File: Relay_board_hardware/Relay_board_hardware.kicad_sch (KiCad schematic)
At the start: 6 parts, among them U1 FTR-F1A, U2 FTR-F1A

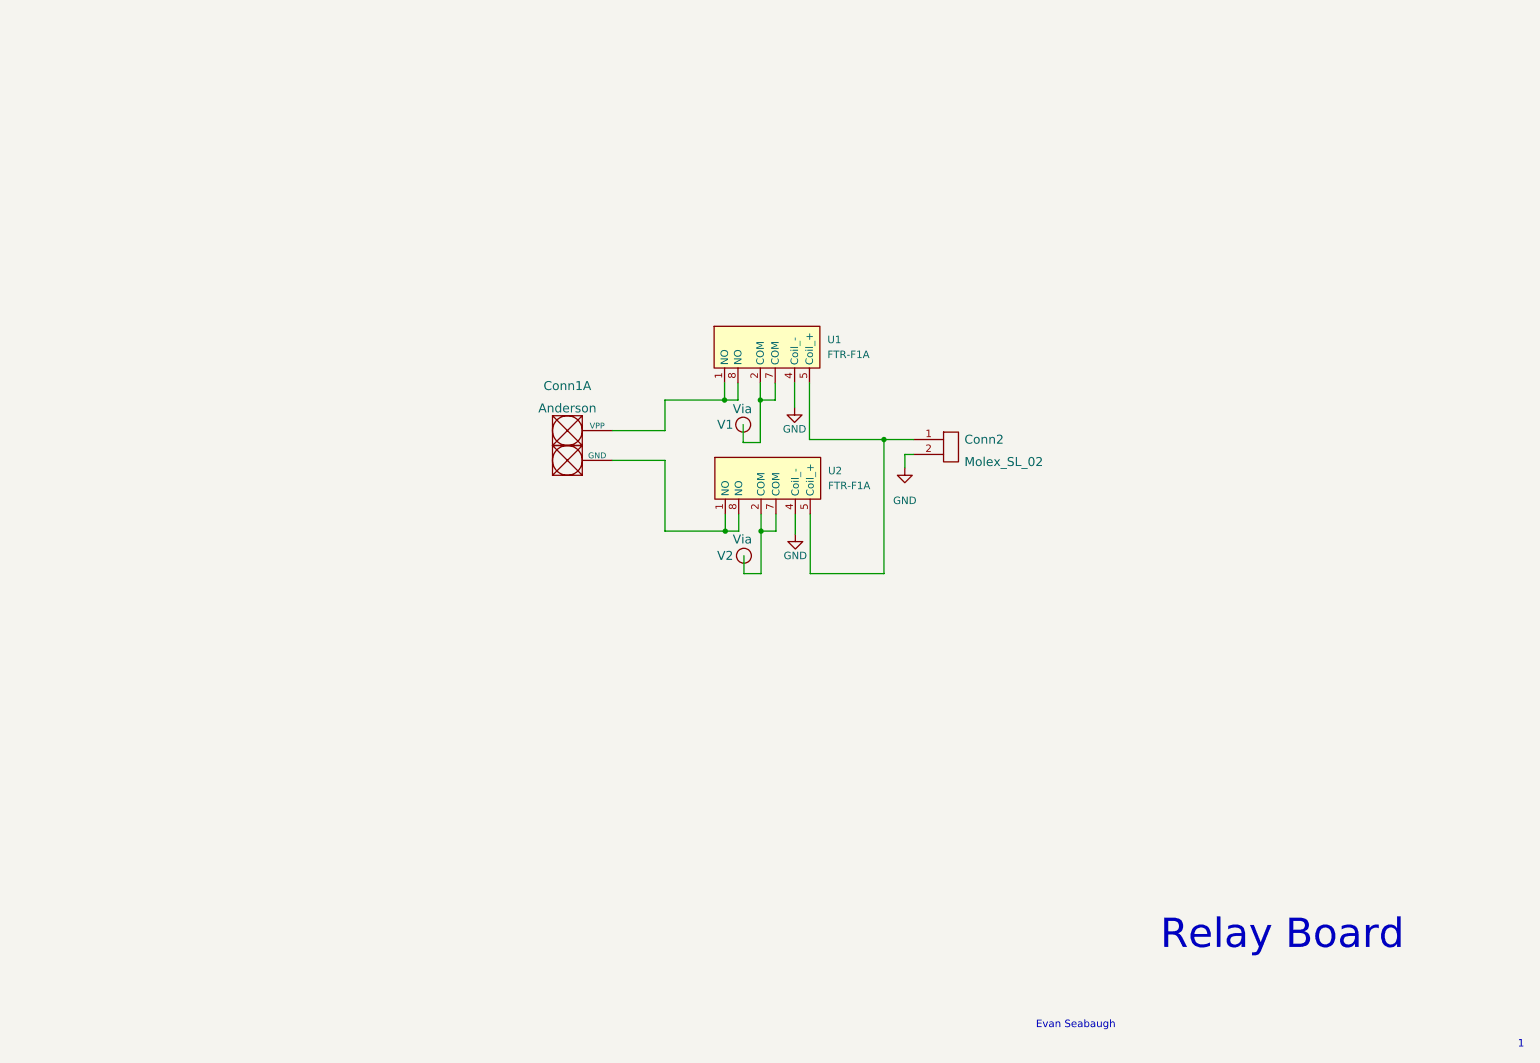
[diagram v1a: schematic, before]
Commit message: board R1
potential changes: anderson placement, IO location, warning correction
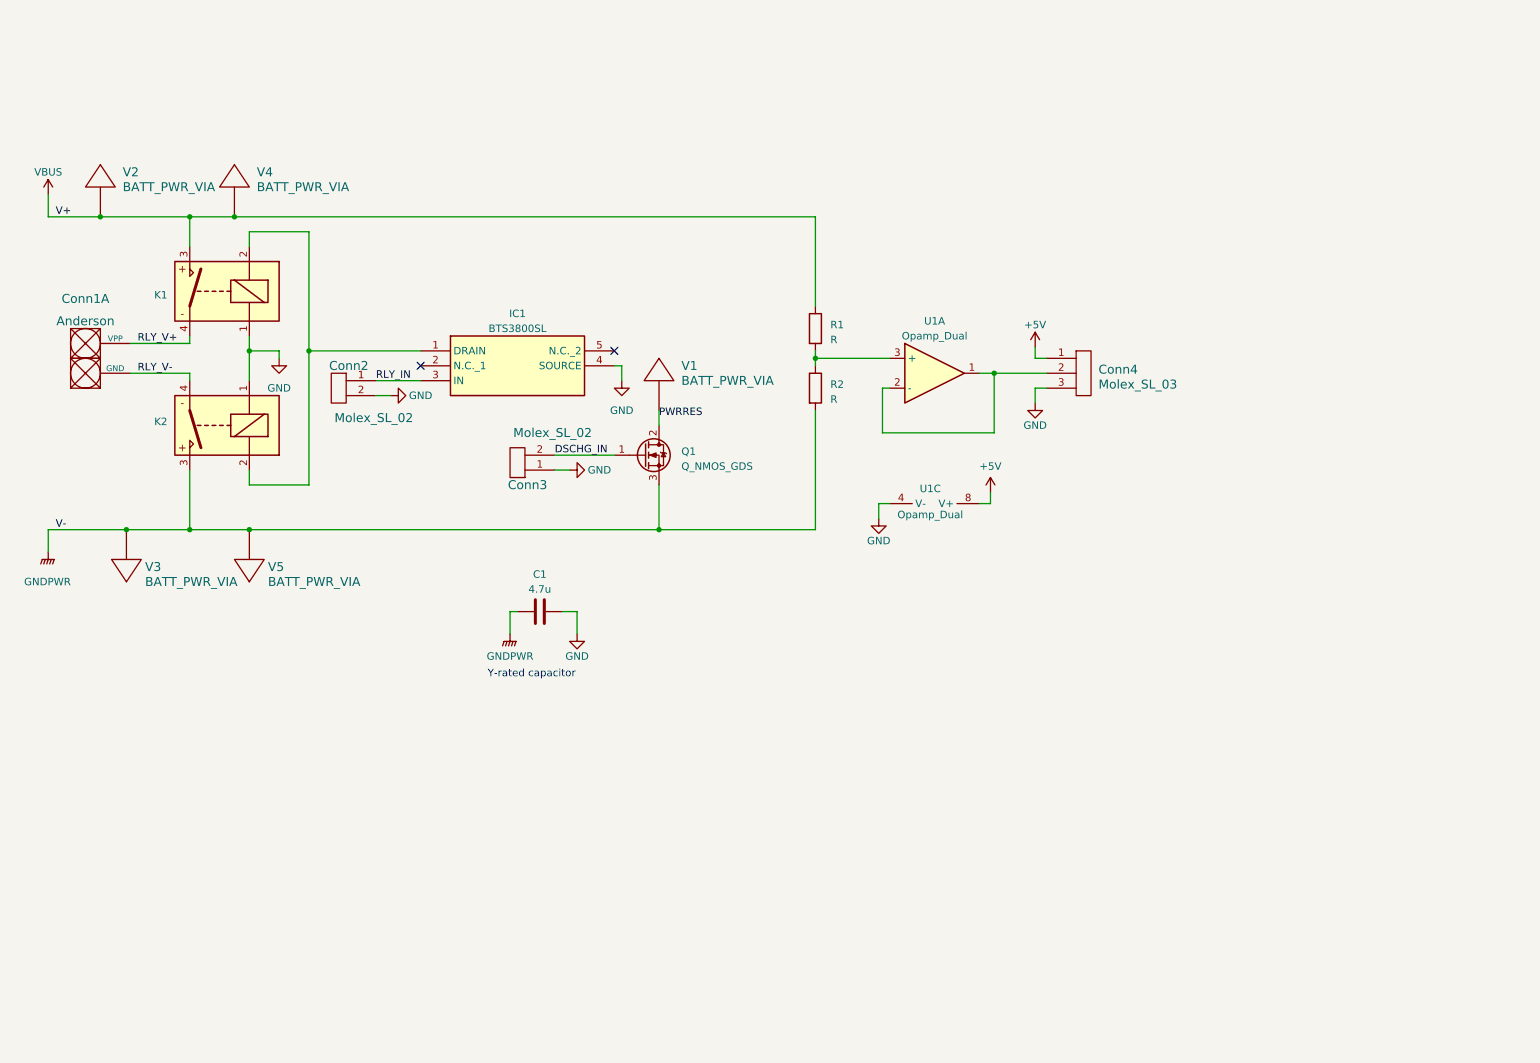
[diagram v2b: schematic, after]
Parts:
- removed Conn2: Molex_SL_02, Customs:MOLEX_SL_02_Horizontal, symbol Customs:Molex_SL_02
- removed U1, U2: FTR-F1A, Customs:FTR-F1A, symbol Customs:FTR-F1A
- removed V1, V2: Via, Customs:via, symbol Customs:Via
- added C1: 4.7u, Capacitor_THT:C_Rect_L18.0mm_W9.0mm_P15.00mm_FKS3_FKP3, symbol Device:C
- added Conn2, Conn3: Molex_SL_02, 0-customs:MOLEX_SL_02_Horizontal, symbol 0-customs:Molex_SL_02
- added Conn4: Molex_SL_03, MRDT_Connectors:MOLEX_SL_03_Horizontal, symbol MRDT_Connectors:Molex_SL_03
- added IC1: BTS3800SL, 0-customs:BTS3800SL, symbol 0-customs:BTS3800SL
- added K1, K2: ~, 0-customs:AECN11012, symbol 0-customs:AECN11012
- added Q1: Q_NMOS_GDS, Package_TO_SOT_SMD:TO-263-2, symbol Device:Q_NMOS_GDS
- added R1, R2: R, Resistor_SMD:R_2512_6332Metric_Pad1.40x3.35mm_HandSolder, symbol Device:R
- added U1: Opamp_Dual, Package_SO:SOIC-8_3.9x4.9mm_P1.27mm, symbol Device:Opamp_Dual
- added V1, V2, V3, V4, V5: BATT_PWR_VIA, 0-customs:via, symbol MRDT_Drill_Holes:BATT_PWR_VIA
- Conn1: footprint Customs:Anderson_2_Vertical_Sidy_by_Side -> 0-customs:Square_Anderson_2_V_Side_By_Side
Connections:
- net GND: now also C1.2, Conn2.2, Conn3.1, Conn4.3, IC1.4 (SOURCE), K1.1, K2.1, U1.4 (V-)
- net RLY_V+: now reaches Conn1.1 (VPP)
- net RLY_V+: now also K1.4
- net RLY_V-: now reaches Conn1.2 (GND)
- net RLY_V-: now also K2.4
- new net: Conn4.2, U1.1, U1.2 (-)
- new net: IC1.1 (DRAIN), K1.2, K2.2
- new net: R1.2, R2.1, U1.3 (+)
- new net +5V: Conn4.1, U1.8 (V+)
- new net DSCHG_IN: Conn3.2, Q1.1 (G)
- new net GNDPWR: C1.1, K2.3, Q1.3 (S), R2.2, V3.1, V5.1
- new net PWRRES: Q1.2 (D), V1.1
- new net RLY_IN: Conn2.1, IC1.3 (IN)
- new net VBUS: K1.3, R1.1, V2.1, V4.1
- no-connect marks 0 -> 2
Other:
- note added: "Y-rated capacitor"
- note removed: "1"
- note removed: "Evan Seabaugh"
- note removed: "Relay Board"
- company: (none) -> Missouri S&T
- title: (none) -> Relay and Connections Board
- moved on the sheet: Conn1A

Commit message: side-by-side-R1
complete board design with the relays situated side-by-side
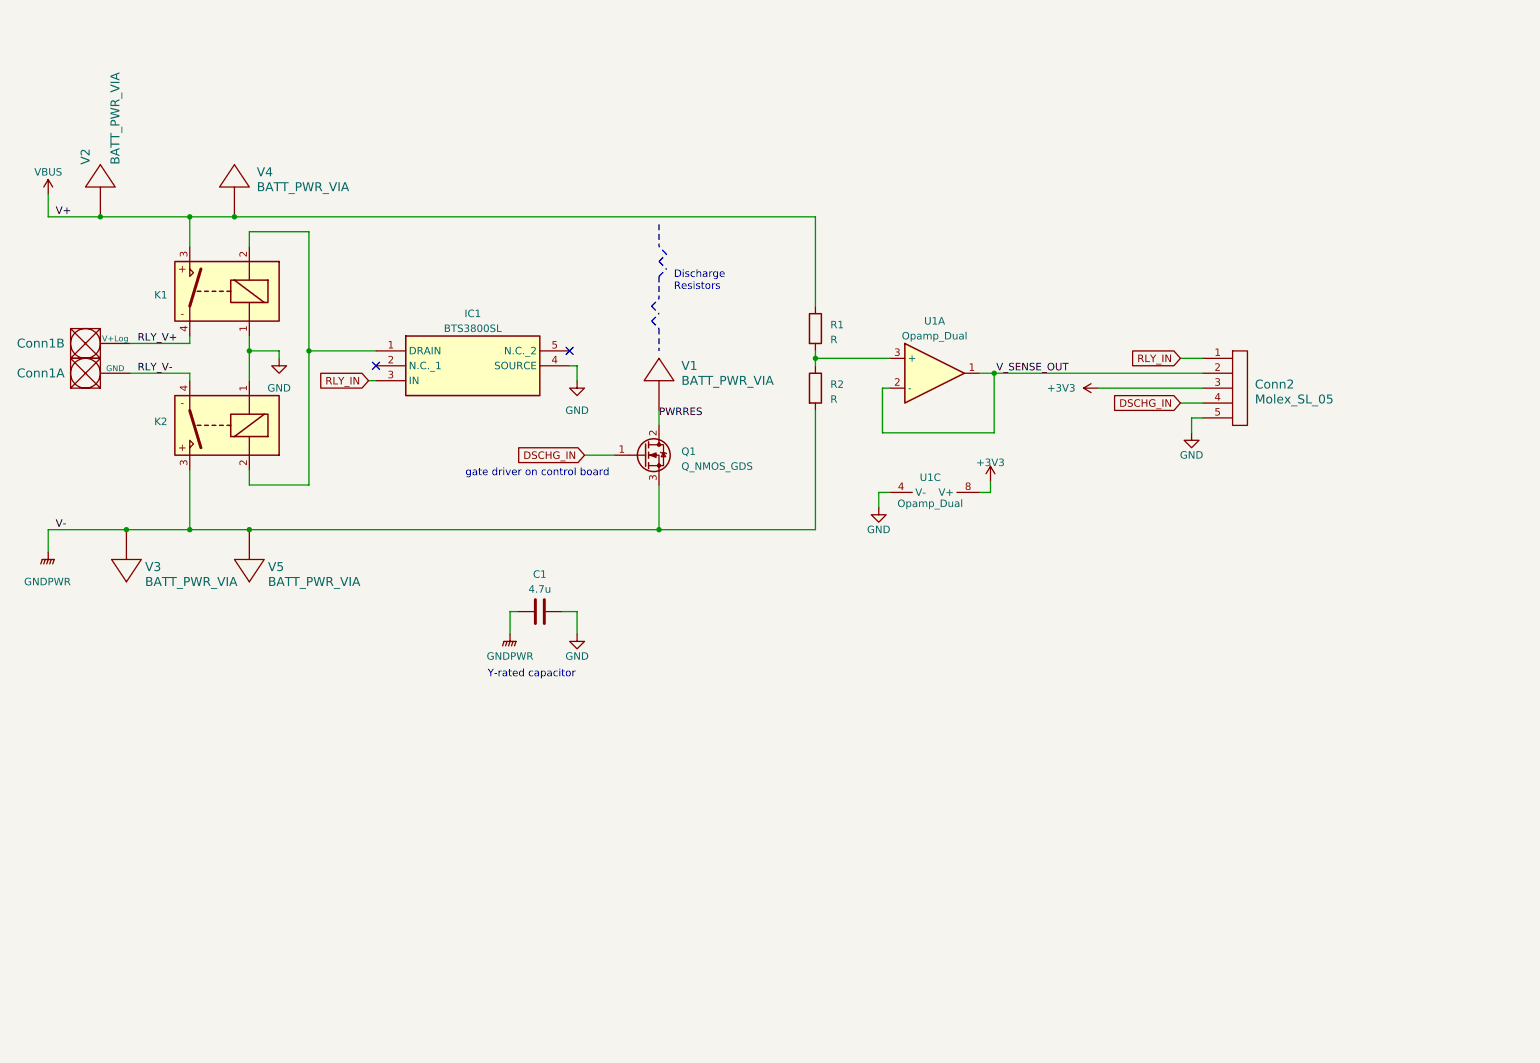
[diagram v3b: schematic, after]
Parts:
- removed Conn1: Anderson, 0-customs:Square_Anderson_2_V_Side_By_Side, symbol Customs:Anderson
- removed Conn2, Conn3: Molex_SL_02, 0-customs:MOLEX_SL_02_Horizontal, symbol 0-customs:Molex_SL_02
- removed Conn4: Molex_SL_03, MRDT_Connectors:MOLEX_SL_03_Horizontal, symbol MRDT_Connectors:Molex_SL_03
- added Conn1: AndersonPP, 0-customs:Square_Anderson_2_H_Side_By_Side, symbol MRDT_Connectors:AndersonPP
- added Conn2: Molex_SL_05, 0-customs:MOLEX_SL_05_Horizontal, symbol 0-customs:Molex_SL_05
- C1: footprint Capacitor_THT:C_Rect_L18.0mm_W9.0mm_P15.00mm_FKS3_FKP3 -> Capacitor_THT:C_Rect_L13.0mm_W5.0mm_P10.00mm_FKS3_FKP3_MKS4
- V1: footprint 0-customs:via -> 0-customs:via_L1000mil_W1000mil
- V2, V3, V4, V5: footprint 0-customs:via -> 0-customs:via_L2500mil_W1000mil
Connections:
- net DSCHG_IN: now also Conn2.4
- net GND: now also Conn2.5
- net RLY_IN: now also Conn2.1
- net RLY_V+: now also Conn1.2 (V+Log)
- net RLY_V-: now also Conn1.1 (GND)
- net V_SENSE_OUT: now reaches U1.1, U1.2 (-)
- net V_SENSE_OUT: now also Conn2.2
- net +5V renamed +3V3
- net +3V3: now also Conn2.3
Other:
- note added: "Discharge Resistors"
- note added: "gate driver on control board"
- moved on the sheet: IC1, U1C

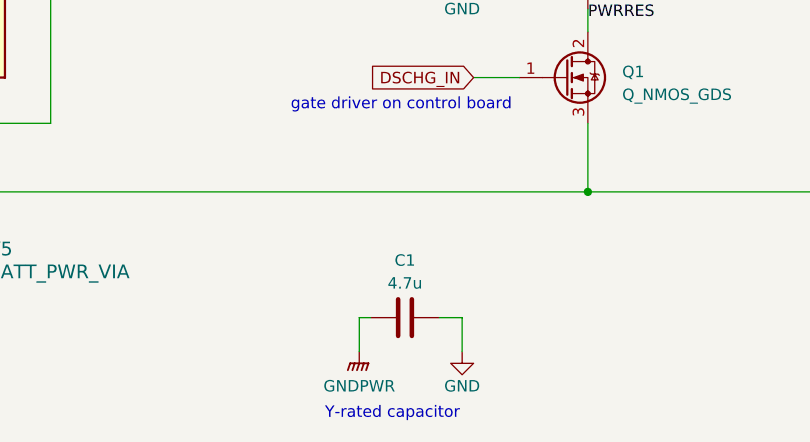
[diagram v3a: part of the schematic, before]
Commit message: board review changes made
major revisions: curved corners, relocated DSCHG resistor pad, cosmetics. Final dimensions 4x4"
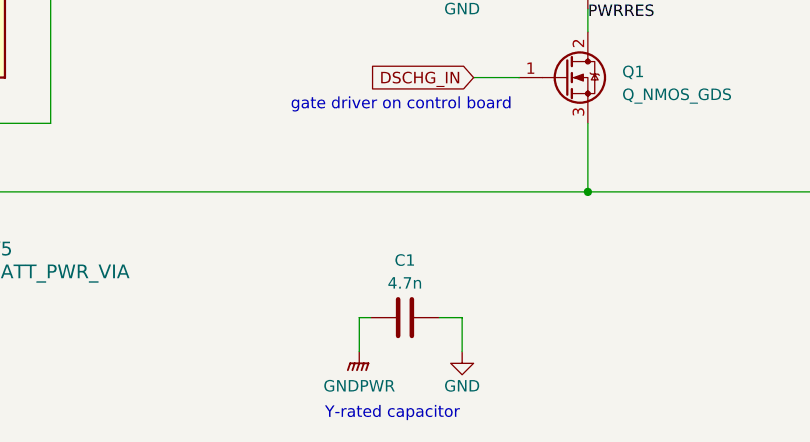
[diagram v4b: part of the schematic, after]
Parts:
- C1: value 4.7u -> 4.7n
- V2, V3, V4, V5: footprint 0-customs:via_L2500mil_W1000mil -> 0-customs:via_L2000mil_W1000mil
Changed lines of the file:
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@@
       (effects (font (size 1.524 1.524)) (justify right))
     )
-    (property "Footprint" "0-customs:via_L2500mil_W1000mil" (at 33.655 110.49 0)
+    (property "Footprint" "0-customs:via_L2000mil_W1000mil" (at 33.655 110.49 0)
       (effects (font (size 1.524 1.524)) hide)
     )
@@
       (effects (font (size 1.27 1.27)))
     )
-    (property "Value" "4.7u" (at 104.14 115.57 90)
+    (property "Value" "4.7n" (at 104.14 115.57 90)
       (effects (font (size 1.27 1.27)))
     )
@@
       (effects (font (size 1.524 1.524)) (justify right))
     )
-    (property "Footprint" "0-customs:via_L2500mil_W1000mil" (at 54.61 110.49 0)
+    (property "Footprint" "0-customs:via_L2000mil_W1000mil" (at 54.61 110.49 0)
       (effects (font (size 1.524 1.524)) hide)
     )
@@
       (effects (font (size 1.524 1.524)) (justify left))
     )
-    (property "Footprint" "0-customs:via_L2500mil_W1000mil" (at 29.21 46.99 0)
+    (property "Footprint" "0-customs:via_L2000mil_W1000mil" (at 29.21 46.99 0)
       (effects (font (size 1.524 1.524)) hide)
     )
@@
       (effects (font (size 1.524 1.524)) (justify left))
     )
-    (property "Footprint" "0-customs:via_L2500mil_W1000mil" (at 52.07 46.99 0)
-      (effects (font (size 1.524 1.524)) hide)
-    )
+    (property "Footprint" "0-customs:via_L2000mil_W1000mil" (at 52.07 46.99 0)
+      (effects (font (size 1.524 1.524)) hide)
+    )

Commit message: bom generated
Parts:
- Q1: value Q_NMOS_GDS -> IRF740ASPBF
- R1: value R -> 650k
- R2: value R -> 5k6
- U1: value Opamp_Dual -> MCP6497T-E/SN
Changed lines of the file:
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@@
       (effects (font (size 1.27 1.27)) (justify left))
     )
-    (property "Value" "Opamp_Dual" (at 165.1 100.965 90)
+    (property "Value" "MCP6497T-E/SN" (at 165.1 100.965 90)
       (effects (font (size 1.27 1.27)) (justify left))
     )
@@
       (effects (font (size 1.27 1.27)) hide)
     )
-    (property "Datasheet" "~" (at 171.45 101.6 0)
+    (property "Datasheet" "https://www.mouser.com/ProductDetail/Microchip-Technology/MCP6497T-E-SN?qs=8Wlm6%252BaMh8Sq3ZIB9JIi0Q%3D%3D" (at 171.45 101.6 0)
       (effects (font (size 1.27 1.27)) hide)
     )
@@
       (effects (font (size 1.27 1.27)) hide)
     )
-    (property "Datasheet" "~" (at 104.14 119.38 0)
+    (property "Datasheet" "https://www.mouser.com/ProductDetail/KEMET/R60QF14704001K?qs=w%2Fv1CP2dgqrzz3BW9Lijdg%3D%3D" (at 104.14 119.38 0)
       (effects (font (size 1.27 1.27)) hide)
     )
@@
       (effects (font (size 1.27 1.27)) (justify left top) hide)
     )
-    (property "Datasheet" "https://componentsearchengine.com/Datasheets/2/BTS3800SL.pdf" (at 105.41 269.85 0)
+    (property "Datasheet" "https://www.mouser.com/ProductDetail/Infineon-Technologies/BTS3800SL?qs=UlfnwZ2x8nQzRqUMCLT9CA%3D%3D" (at 105.41 269.85 0)
       (effects (font (size 1.27 1.27)) (justify left top) hide)
     )
@@
       (effects (font (size 1.27 1.27)))
     )
-    (property "Value" "Opamp_Dual" (at 171.45 72.39 0)
+    (property "Value" "MCP6497T-E/SN" (at 171.45 72.39 0)
       (effects (font (size 1.27 1.27)))
     )
@@
       (effects (font (size 1.27 1.27)) hide)
     )
-    (property "Datasheet" "~" (at 171.45 78.74 0)
+    (property "Datasheet" "https://www.mouser.com/ProductDetail/Microchip-Technology/MCP6497T-E-SN?qs=8Wlm6%252BaMh8Sq3ZIB9JIi0Q%3D%3D" (at 171.45 78.74 0)
       (effects (font (size 1.27 1.27)) hide)
     )
@@
       (effects (font (size 1.27 1.27)) (justify left))
     )
-    (property "Value" "Q_NMOS_GDS" (at 128.27 94.615 0)
+    (property "Value" "IRF740ASPBF" (at 128.27 94.615 0)
       (effects (font (size 1.27 1.27)) (justify left))
     )
@@
       (effects (font (size 1.27 1.27)) hide)
     )
-    (property "Datasheet" "~" (at 121.92 92.71 0)
+    (property "Datasheet" "https://www.mouser.com/ProductDetail/Vishay-Semiconductors/IRF740ASPBF?qs=I1ZA2VTqfvSWXSCbb2jmeg%3D%3D" (at 121.92 92.71 0)
       (effects (font (size 1.27 1.27)) hide)
     )
@@
       (effects (font (size 1.27 1.27)) (justify left))
     )
-    (property "Value" "R" (at 153.67 83.185 0)
+    (property "Value" "5k6" (at 153.67 83.185 0)
       (effects (font (size 1.27 1.27)) (justify left))
     )
@@
       (effects (font (size 1.27 1.27)) hide)
     )
-    (property "Datasheet" "~" (at 151.13 81.28 0)
+    (property "Datasheet" "https://www.mouser.com/ProductDetail/Vishay-Dale/CRCW25125K60FKEG?qs=WpL82mpZNv%252BDAPMX1UK%2Frw%3D%3D" (at 151.13 81.28 0)
       (effects (font (size 1.27 1.27)) hide)
     )
@@
       (effects (font (size 1.27 1.27)) (justify left))
     )
-    (property "Value" "R" (at 153.67 73.025 0)
+    (property "Value" "650k" (at 153.67 73.025 0)
       (effects (font (size 1.27 1.27)) (justify left))
     )
@@
       (effects (font (size 1.27 1.27)) hide)
     )
-    (property "Datasheet" "~" (at 151.13 71.12 0)
-      (effects (font (size 1.27 1.27)) hide)
-    )
+    (property "Datasheet" "https://www.mouser.com/ProductDetail/Vishay-Dale/CRCW2512649KFKEG?qs=WpL82mpZNv9YmPWivNEPLA%3D%3D" (at 151.13 71.12 0)
+      (effects (font (size 1.27 1.27)) hide)
+    )
